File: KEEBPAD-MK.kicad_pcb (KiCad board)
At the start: 4 copper layers, 112.5 x 81.2 mm, 32 parts, among them J1 SH1106G, J2 USB_C_Receptacle_USB2.0, SW1 SW_SPST, SW2 SW_SPST, SW3 SW_SPST, SW4 SW_SPST, SW5 SW_SPST, SW6 SW_SPST, SW7 SW_SPST, SW8 SW_SPST

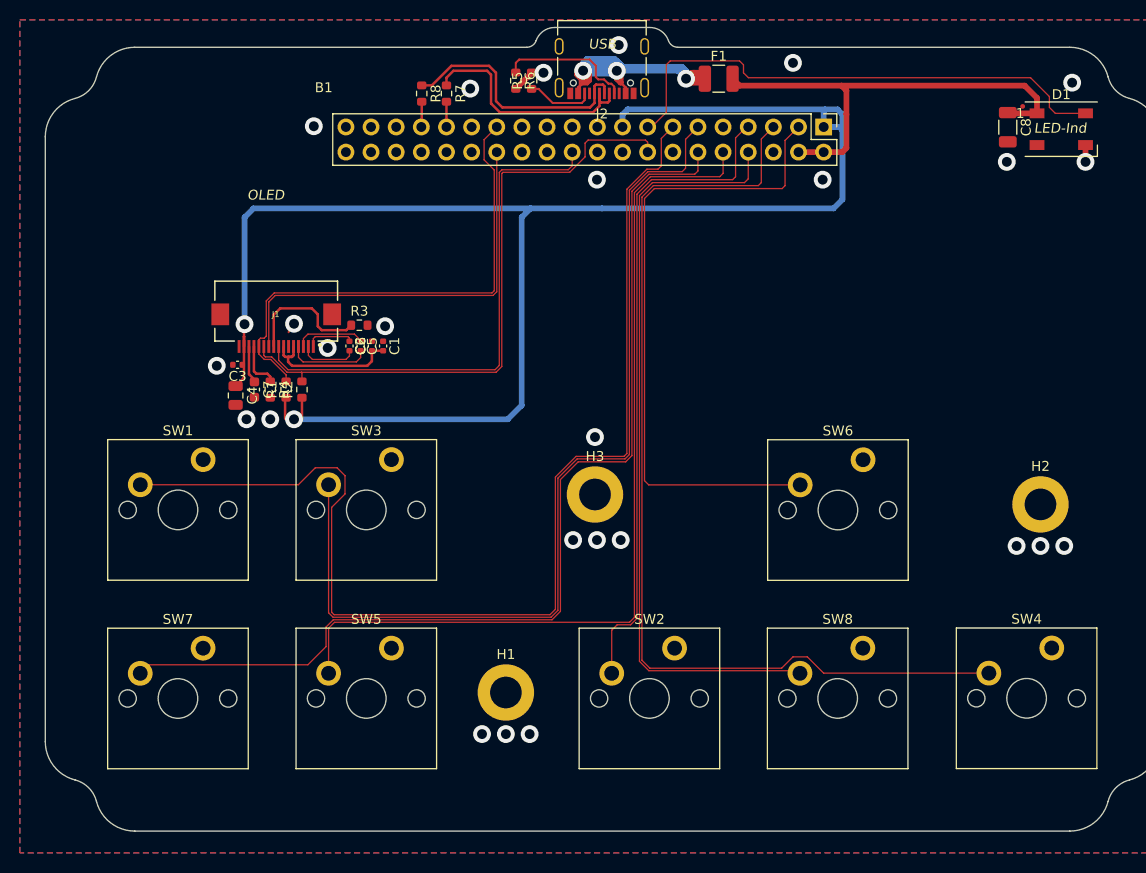
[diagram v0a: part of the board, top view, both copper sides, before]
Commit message: Fixed SPI pin assignments to SPI0 only
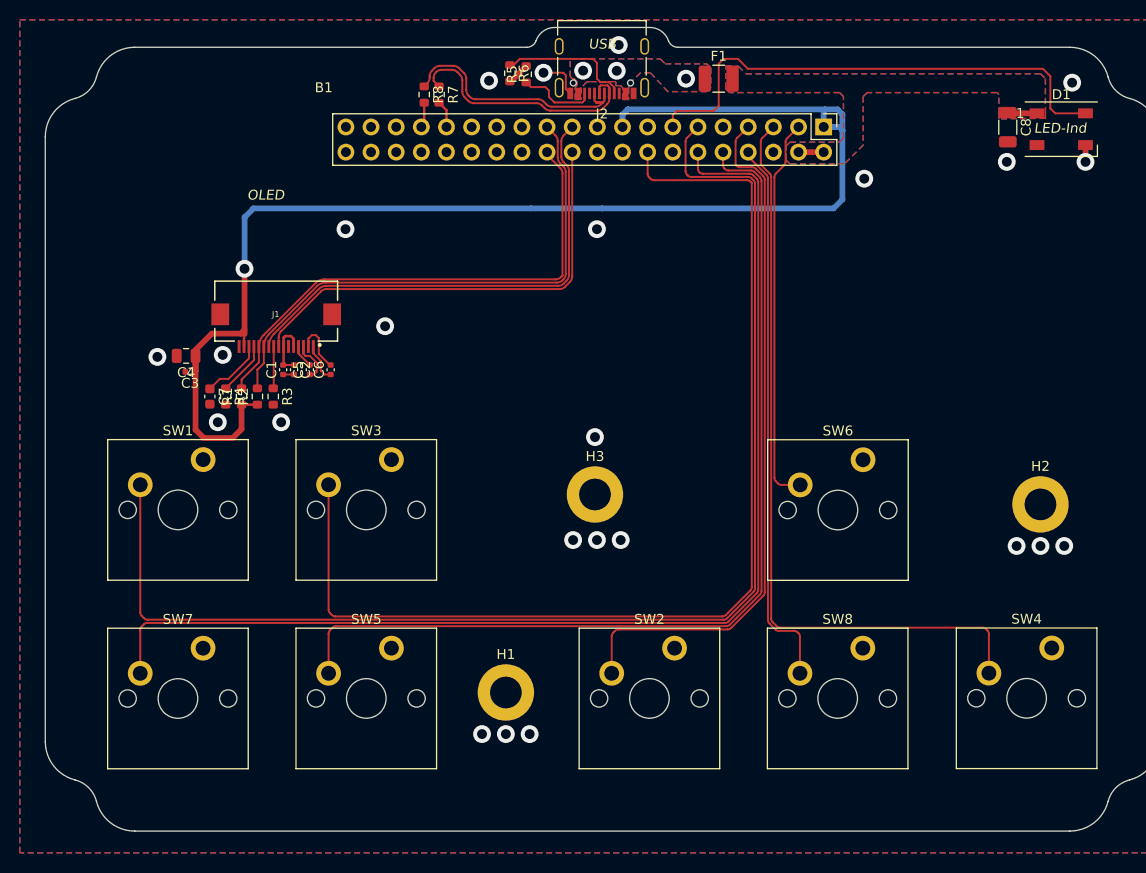
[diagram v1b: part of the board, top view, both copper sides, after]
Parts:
- moved R3 11.3 mm to (117.5, 140.1), turned to -90 degrees
- moved C1 10.4 mm to (118.5, 137.4), turned to 90 degrees
- moved C2 8.22 mm to (119.6, 137.4), turned to -90 degrees
- moved C4 6.40 mm to (108.7, 136.0), turned to 180 degrees
- moved C5 5.67 mm to (121.2, 137.4), turned to 90 degrees
- moved C3 4.85 mm to (109.1, 137.6)
- moved C7 4.55 mm to (111.1, 140.1)
- moved R1 4.55 mm to (114.3, 140.1)
- moved R2 4.55 mm to (115.9, 140.1)
- moved R4 4.55 mm to (112.7, 140.1)
- moved C6 3.06 mm to (123.3, 137.4), turned to 90 degrees
- moved R6 0.96 mm to (141.4, 107.5)
- moved R5 0.85 mm to (143.1, 107.5)
- moved R7 0.76 mm to (134.2, 109.6)
- moved R8 0.27 mm to (132.8, 109.6)
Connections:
- net /Pinheader Assignments/$.USB_{VBUS}_DET renamed /Pinheader Assignments/$.GPIO_{9}
- net /Pinheader Assignments/$.USB_{VBUS}_ENABLE renamed /Pinheader Assignments/$.GPIO_{6}
- B1 pad 16: /Pinheader Assignments/$.SPI^{0}_{SCK} -> /Pinheader Assignments/$.GPIO_{22}
- B1 pad 23: /Pinheader Assignments/$.GPIO_{18} -> /Pinheader Assignments/$.SPI^{0}_{SCK}
- B1 pad 24: /Pinheader Assignments/$.GPIO_{19} -> /Pinheader Assignments/$.SPI^{0}_{TX}
- B1 pad 27: /Pinheader Assignments/$.SPI^{0}_{TX} -> /Pinheader Assignments/$.GPIO_{15}
- D1 pad 4: /Pinheader Assignments/$.GPIO_{25} -> /Pinheader Assignments/$.ADC_{0}
- J1 pad 10: /Pinheader Assignments/$.GPIO_{16} -> /Pinheader Assignments/$.GPIO_{20}
- SW1 pad 1: /Pinheader Assignments/$.ADC_{0} -> /Pinheader Assignments/$.ADC_{1}
- SW3 pad 1: /Pinheader Assignments/$.ADC_{1} -> /Pinheader Assignments/$.GPIO_{22}
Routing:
- net /Pinheader Assignments/$.GPIO_{22}: track 0.00 -> 111.0 mm
- net /Pinheader Assignments/$.ADC_{0}: track 116.1 -> 51.9 mm
- net Net-(F1-Pad1): track 56.9 -> 0.00 mm
- net /Pinheader Assignments/$.GPIO_{25}: track 53.1 -> 0.00 mm
- net /Pinheader Assignments/$.GPIO_{20}: track 0.00 -> 49.4 mm
- net VBUS: track 47.6 -> 5.52 mm
- net /Pinheader Assignments/$.GPIO_{16}: track 42.1 -> 0.22 mm
- net /Pinheader Assignments/$.ADC_{1}: track 96.1 -> 130.3 mm
- net +3V3: track 167.7 -> 135.4 mm, vias 2 -> 1
- net /Pinheader Assignments/$.B: track 65.6 -> 39.4 mm
- net /Pinheader Assignments/$.START: track 102.1 -> 77.3 mm
- net /Pinheader Assignments/$.SELECT: track 78.1 -> 55.8 mm
- net /Pinheader Assignments/$.ADC_{2}: track 103.9 -> 118.3 mm
- net /Pinheader Assignments/$.SPI^{0}_{SCK}: track 64.4 -> 53.9 mm
- net /128x64 OLED Display/VBAT: track 14.8 -> 5.86 mm
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- added copper zone on B.Cu, net Net-(F1-Pad1)
- added copper zone on F.Cu, net Net-(F1-Pad1)
- added copper zone on B.Cu, net VBUS
- added copper zone on F.Cu, net VBUS
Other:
- board text added: "FIDUCIAL"
- board text removed: "CHANGE"

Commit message: 
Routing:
- net /Pinheader Assignments/$.SPI^{0}_{TX}: track 52.4 -> 55.4 mm
- net /Pinheader Assignments/$.SPI^{0}_{~{CS}}: track 45.9 -> 48.8 mm
- net /Pinheader Assignments/$.SPI^{0}_{SCK}: track 53.9 -> 56.4 mm
- net /Pinheader Assignments/$.GPIO_{20}: track 49.4 -> 51.6 mm
- net /Pinheader Assignments/$.GPIO_{22}: track 111.0 -> 112.6 mm
- net /Pinheader Assignments/$.ADC_{1}: track 130.3 -> 131.9 mm
- net /Pinheader Assignments/$.ADC_{2}: track 118.3 -> 119.8 mm
- net /Pinheader Assignments/$.ADC_{3}: track 97.1 -> 98.6 mm
- net /Pinheader Assignments/$.GPIO_{6}: track 70.8 -> 72.2 mm
- net /128x64 OLED Display/VCOM_{H}: track 6.42 -> 7.78 mm
- net /128x64 OLED Display/IREF: track 5.41 -> 6.65 mm
- net GND: track 9.47 -> 8.37 mm, vias 24 -> 12
- removed copper zone on B.Cu, net VBUS
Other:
- board text added: "HT-SIN"
- board text added: "MICL.DEV"
